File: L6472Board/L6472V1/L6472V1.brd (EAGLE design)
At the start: 76.2 x 76.2 mm, 34 parts

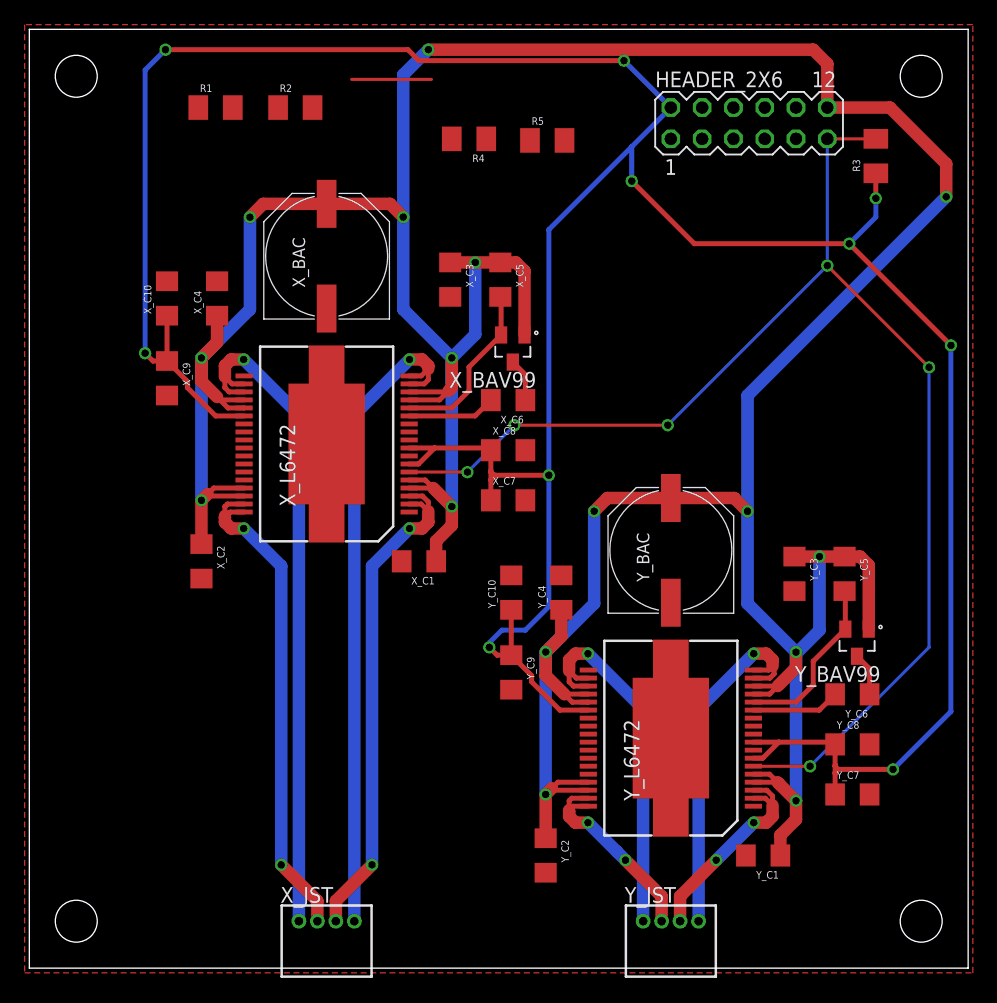
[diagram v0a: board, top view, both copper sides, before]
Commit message: Completed Routing of PCB
The layout of the L6472 PCB was completed.
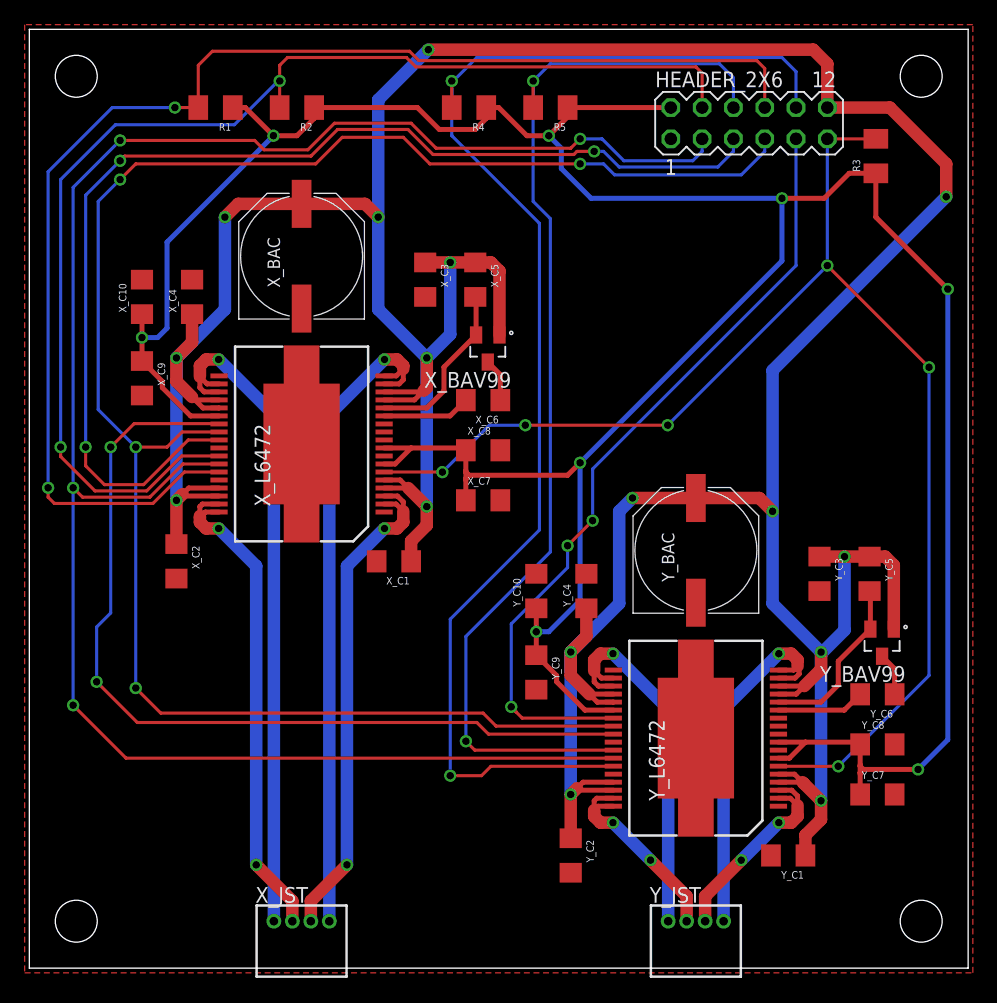
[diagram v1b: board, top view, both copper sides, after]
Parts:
- moved R5 2.68 mm to (42.3, 69.8), turned to 180 degrees
- moved R4 2.54 mm to (35.7, 69.8)
- moved Y_C10 2.04 mm to (41.1, 30.6)
- moved Y_C4 2.04 mm to (45.2, 30.6)
- moved X_C10 2.04 mm to (9.14, 54.5)
- moved X_C4 2.04 mm to (13.2, 54.5)
- moved X_BAV99 2.03 mm to (37.2, 50.3)
- moved X_C6 2.03 mm to (36.8, 46.1)
- moved X_C7 2.03 mm to (36.8, 38.0)
- moved X_C8 2.03 mm to (36.8, 42.0)
- moved Y_C2 2.03 mm to (43.9, 9.14)
- moved Y_C3 2.03 mm to (64.1, 32.0)
- moved Y_C9 2.03 mm to (41.1, 24.0)
- moved X_BAC 2.03 mm to (22.1, 57.8)
- moved X_C1 2.03 mm to (29.6, 33.0)
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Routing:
- net CS: track 0.00 -> 158.0 mm, vias 0 -> 4
- net CLK: track 0.00 -> 147.4 mm, vias 0 -> 4
- net Y_FLAG: track 0.00 -> 110.2 mm, vias 0 -> 2
- net X_FLAG: track 0.00 -> 109.5 mm, vias 0 -> 2
- net X_BUSY: track 0.00 -> 100.1 mm, vias 0 -> 2
- net MOSI: track 0.00 -> 92.7 mm, vias 0 -> 3
- net Y_BUSY: track 0.00 -> 91.2 mm, vias 0 -> 2
- net DAISY: track 0.00 -> 72.8 mm, vias 0 -> 2
- net MISO: track 0.00 -> 64.4 mm, vias 0 -> 3
- net N$2: track 6.48 -> 0.00 mm
- net VDD: track 261.6 -> 256.5 mm, vias 10 -> 8
- net STBY: track 107.8 -> 109.1 mm

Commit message: Final motor controller
This is the final layout of the motor controller board before
manufacturing.
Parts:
- moved X_C1 3.56 mm to (29.6, 29.5)
- moved X_C2 3.05 mm to (11.9, 30.0)
- moved Y_C3 2.79 mm to (64.1, 34.8)
- moved Y_C5 2.79 mm to (68.2, 34.8)
- moved Y_BAV99 2.79 mm to (69.2, 29.2)
- moved X_BAV99 2.79 mm to (37.2, 53.1)
- moved X_C3 2.79 mm to (32.1, 58.7)
- moved X_C5 2.79 mm to (36.2, 58.7)
- moved Y_C1 2.54 mm to (61.6, 6.60)
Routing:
- net VS: track 350.1 -> 364.9 mm
- net Y_VBOOT: track 14.2 -> 17.0 mm
- net X_VBOOT: track 14.2 -> 17.0 mm
- net X_C1: track 3.51 -> 6.31 mm
- net X_C6: track 3.51 -> 6.31 mm
- net X_2B: track 54.5 -> 56.8 mm
- net Y_2B: track 30.5 -> 32.8 mm
- net X_1B: track 53.8 -> 56.1 mm
- net Y_1B: track 30.5 -> 32.8 mm
- net X_2A: track 40.7 -> 40.1 mm
- net X_1A: track 41.3 -> 40.7 mm
- net Y_2A: track 16.9 -> 16.3 mm
- net Y_1A: track 17.4 -> 16.8 mm
- net MISO: track 64.4 -> 64.9 mm
- added copper zone on layer 16, net N$2
